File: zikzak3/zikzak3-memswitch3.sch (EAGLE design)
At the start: 45 parts, among them IC2 MEGA128-A, Q1 16MHz, Q2 20MHz

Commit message: updated schematic
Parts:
- added BUFFER3: 74LS245N, 74xx-us:74LS245N
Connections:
- new net N$105: BUFFER3A.A2, MUX10A.2Y
- new net N$106: BUFFER3A.A1, MUX10A.1Y
- new net N$109: BUFFER3A.A5, MUX9A.1Y
- new net N$11: BUFFER3A.A4, MUX10A.4Y
- new net N$110: BUFFER3A.A6, MUX9A.2Y
- new net N$111: BUFFER3A.A7, MUX9A.3Y
- new net N$112: BUFFER3A.A8, MUX9A.4Y
- new net N$12: MUX10A.3Y
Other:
- moved on the sheet: R10, R3, R4, R5, R6, R7, R8, R9
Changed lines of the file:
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@@
 <setting verticaltext="up"/>
 </settings>
-<grid distance="0.1" unitdist="inch" unit="inch" style="dots" multiple="1" display="yes" altdistance="0.01" altunitdist="inch" altunit="inch"/>
+<grid distance="0.1" unitdist="inch" unit="inch" style="lines" multiple="1" display="no" altdistance="0.01" altunitdist="inch" altunit="inch"/>
 <layers>
 <layer number="1" name="Top" color="4" fill="1" visible="no" active="no"/>
@@
 <part name="R10" library="rcl" deviceset="R-US_" device="0204/2V"/>
 <part name="INVERTOR" library="74xx-us" deviceset="74*04" device="N" technology="LS"/>
+<part name="BUFFER3" library="74xx-us" deviceset="74*245" device="N" technology="LS"/>
 </parts>
 <sheets>
@@
 <text x="243.84" y="63.5" size="6.4516" layer="91">GPU (Sync Gen)</text>
 <text x="302.26" y="-294.64" size="6.4516" layer="91">VGA</text>
-<text x="238.76" y="-294.64" size="6.4516" layer="91">DAC</text>
+<text x="266.7" y="-302.26" size="6.4516" layer="91">DAC</text>
 <text x="167.64" y="-299.72" size="6.4516" layer="91">VID SW</text>
 <text x="-170.18" y="-170.18" size="1.778" layer="91">INVERT</text>
@@
 <instance part="P+4" gate="1" x="30.48" y="-172.72"/>
 <instance part="GND14" gate="1" x="35.56" y="-154.94" rot="R180"/>
-<instance part="R3" gate="G$1" x="246.38" y="-228.6" rot="MR0"/>
-<instance part="R4" gate="G$1" x="246.38" y="-233.68" rot="MR0"/>
-<instance part="R5" gate="G$1" x="246.38" y="-243.84" rot="MR0"/>
-<instance part="R6" gate="G$1" x="246.38" y="-248.92" rot="MR0"/>
-<instance part="R7" gate="G$1" x="246.38" y="-261.62" rot="MR0"/>
-<instance part="R8" gate="G$1" x="246.38" y="-266.7" rot="MR0"/>
-<instance part="R9" gate="G$1" x="246.38" y="-276.86" rot="MR0"/>
-<instance part="R10" gate="G$1" x="246.38" y="-281.94" rot="MR0"/>
+<instance part="R3" gate="G$1" x="274.32" y="-236.22" rot="MR0"/>
+<instance part="R4" gate="G$1" x="274.32" y="-241.3" rot="MR0"/>
+<instance part="R5" gate="G$1" x="274.32" y="-251.46" rot="MR0"/>
+<instance part="R6" gate="G$1" x="274.32" y="-256.54" rot="MR0"/>
+<instance part="R7" gate="G$1" x="274.32" y="-269.24" rot="MR0"/>
+<instance part="R8" gate="G$1" x="274.32" y="-274.32" rot="MR0"/>
+<instance part="R9" gate="G$1" x="274.32" y="-284.48" rot="MR0"/>
+<instance part="R10" gate="G$1" x="274.32" y="-289.56" rot="MR0"/>
 <instance part="INVERTOR" gate="A" x="-167.64" y="-147.32" rot="R270"/>
+<instance part="BUFFER3" gate="A" x="233.68" y="-256.54"/>
 </instances>
 <busses>
@@
 </segment>
 </net>
-<net name="N$105" class="0">
-<segment>
-<wire x1="190.5" y1="-248.92" x2="236.22" y2="-248.92" width="0.1524" layer="91"/>
-</segment>
-</net>
-<net name="N$106" class="0">
-<segment>
-<wire x1="259.08" y1="-248.92" x2="299.72" y2="-248.92" width="0.1524" layer="91"/>
-</segment>
-</net>
 <net name="N$107" class="0">
 <segment>
@@
 </segment>
 </net>
+<net name="N$11" class="0">
+<segment>
+<pinref part="MUX10" gate="A" pin="4Y"/>
+<wire x1="187.96" y1="-238.76" x2="200.66" y2="-238.76" width="0.1524" layer="91"/>
+<wire x1="200.66" y1="-238.76" x2="200.66" y2="-251.46" width="0.1524" layer="91"/>
+<pinref part="BUFFER3" gate="A" pin="A4"/>
+<wire x1="200.66" y1="-251.46" x2="220.98" y2="-251.46" width="0.1524" layer="91"/>
+</segment>
+</net>
+<net name="N$12" class="0">
+<segment>
+<pinref part="MUX10" gate="A" pin="3Y"/>
+<wire x1="187.96" y1="-233.68" x2="203.2" y2="-233.68" width="0.1524" layer="91"/>
+<wire x1="203.2" y1="-233.68" x2="203.2" y2="-248.92" width="0.1524" layer="91"/>
+<wire x1="203.2" y1="-248.92" x2="223.52" y2="-248.92" width="0.1524" layer="91"/>
+</segment>
+</net>
+<net name="N$105" class="0">
+<segment>
+<pinref part="MUX10" gate="A" pin="2Y"/>
+<wire x1="187.96" y1="-228.6" x2="205.74" y2="-228.6" width="0.1524" layer="91"/>
+<wire x1="205.74" y1="-228.6" x2="205.74" y2="-246.38" width="0.1524" layer="91"/>
+<pinref part="BUFFER3" gate="A" pin="A2"/>
+<wire x1="205.74" y1="-246.38" x2="220.98" y2="-246.38" width="0.1524" layer="91"/>
+</segment>
+</net>
+<net name="N$106" class="0">
+<segment>
+<pinref part="MUX10" gate="A" pin="1Y"/>
+<wire x1="187.96" y1="-223.52" x2="208.28" y2="-223.52" width="0.1524" layer="91"/>
+<wire x1="208.28" y1="-223.52" x2="208.28" y2="-243.84" width="0.1524" layer="91"/>
+<pinref part="BUFFER3" gate="A" pin="A1"/>
+<wire x1="208.28" y1="-243.84" x2="220.98" y2="-243.84" width="0.1524" layer="91"/>
+</segment>
+</net>
+<net name="N$109" class="0">
+<segment>
+<pinref part="MUX9" gate="A" pin="1Y"/>
+<wire x1="200.66" y1="-259.08" x2="200.66" y2="-254" width="0.1524" layer="91"/>
+<pinref part="BUFFER3" gate="A" pin="A5"/>
+<wire x1="200.66" y1="-254" x2="220.98" y2="-254" width="0.1524" layer="91"/>
+</segment>
+</net>
+<net name="N$110" class="0">
+<segment>
+<pinref part="MUX9" gate="A" pin="2Y"/>
+<wire x1="200.66" y1="-264.16" x2="203.2" y2="-264.16" width="0.1524" layer="91"/>
+<wire x1="203.2" y1="-264.16" x2="203.2" y2="-256.54" width="0.1524" layer="91"/>
+<pinref part="BUFFER3" gate="A" pin="A6"/>
+<wire x1="203.2" y1="-256.54" x2="220.98" y2="-256.54" width="0.1524" layer="91"/>
+</segment>
+</net>
+<net name="N$111" class="0">
+<segment>
+<pinref part="MUX9" gate="A" pin="3Y"/>
+<wire x1="200.66" y1="-269.24" x2="205.74" y2="-269.24" width="0.1524" layer="91"/>
+<wire x1="205.74" y1="-269.24" x2="205.74" y2="-259.08" width="0.1524" layer="91"/>
+<pinref part="BUFFER3" gate="A" pin="A7"/>
+<wire x1="205.74" y1="-259.08" x2="220.98" y2="-259.08" width="0.1524" layer="91"/>
+</segment>
+</net>
+<net name="N$112" class="0">
+<segment>
+<pinref part="MUX9" gate="A" pin="4Y"/>
+<wire x1="200.66" y1="-274.32" x2="208.28" y2="-274.32" width="0.1524" layer="91"/>
+<wire x1="208.28" y1="-274.32" x2="208.28" y2="-261.62" width="0.1524" layer="91"/>
+<pinref part="BUFFER3" gate="A" pin="A8"/>
+<wire x1="208.28" y1="-261.62" x2="220.98" y2="-261.62" width="0.1524" layer="91"/>
+</segment>
+</net>

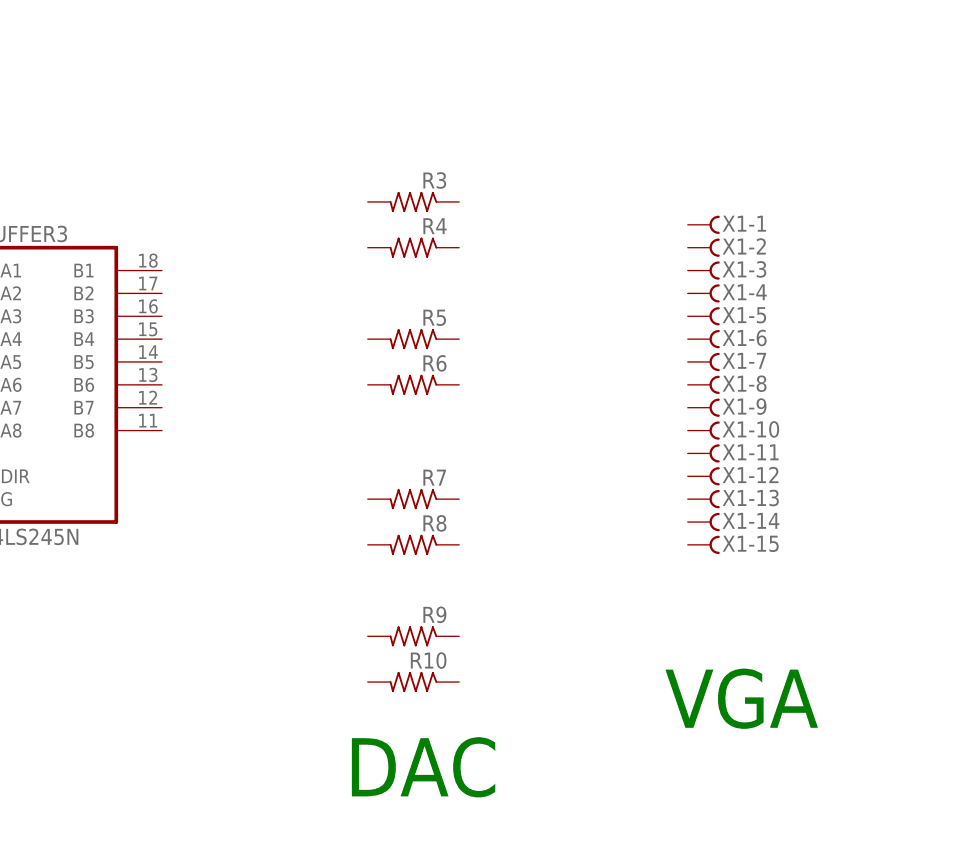
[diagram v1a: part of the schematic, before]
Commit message: schematic update; added DAC details
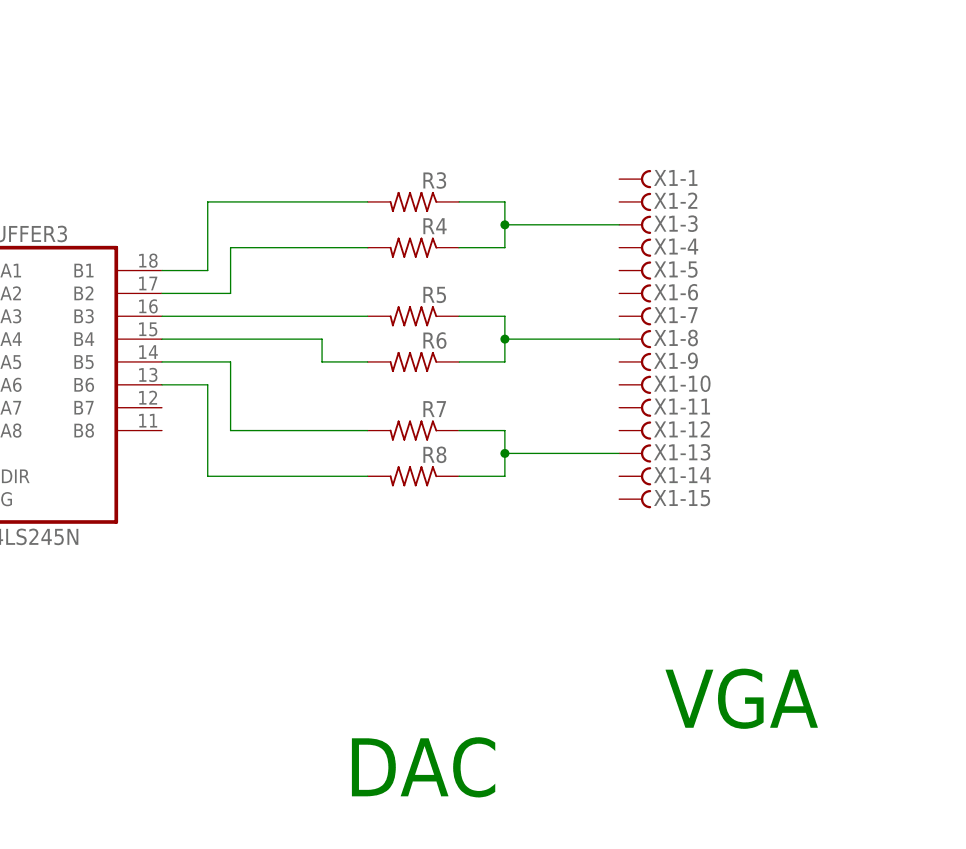
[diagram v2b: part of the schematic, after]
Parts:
- removed R10, R9: (no value), rcl:R-US_0204/2V
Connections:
- new net N$113: BUFFER3A.B1, R3.2
- new net N$114: BUFFER3A.B2, R4.2
- new net N$115: BUFFER3A.B3, R5.2
- new net N$116: BUFFER3A.B4, R6.2
- new net N$117: BUFFER3A.B5, R7.2
- new net N$118: BUFFER3A.B6, R8.2
- new net N$119: R3.1, R4.1, X1-3.F
- new net N$121: R5.1, R6.1, X1-8.F
- new net N$123: R7.1, R8.1, X1-13.F
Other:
- moved on the sheet: R5, R6, R7, R8, X1-1, X1-10, X1-11, X1-12, X1-13, X1-14, X1-15, X1-2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
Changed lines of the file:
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@@
 <part name="R7" library="rcl" deviceset="R-US_" device="0204/2V"/>
 <part name="R8" library="rcl" deviceset="R-US_" device="0204/2V"/>
-<part name="R9" library="rcl" deviceset="R-US_" device="0204/2V"/>
-<part name="R10" library="rcl" deviceset="R-US_" device="0204/2V"/>
 <part name="INVERTOR" library="74xx-us" deviceset="74*04" device="N" technology="LS"/>
 <part name="BUFFER3" library="74xx-us" deviceset="74*245" device="N" technology="LS"/>
@@
 <instance part="P+1" gate="1" x="-322.58" y="124.46" rot="MR0"/>
 <instance part="GND1" gate="1" x="-322.58" y="114.3" rot="MR0"/>
-<instance part="X1" gate="-1" x="307.34" y="-238.76"/>
-<instance part="X1" gate="-2" x="307.34" y="-241.3"/>
-<instance part="X1" gate="-3" x="307.34" y="-243.84"/>
-<instance part="X1" gate="-4" x="307.34" y="-246.38"/>
-<instance part="X1" gate="-5" x="307.34" y="-248.92"/>
-<instance part="X1" gate="-6" x="307.34" y="-251.46"/>
-<instance part="X1" gate="-7" x="307.34" y="-254"/>
-<instance part="X1" gate="-8" x="307.34" y="-256.54"/>
-<instance part="X1" gate="-9" x="307.34" y="-259.08"/>
-<instance part="X1" gate="-10" x="307.34" y="-261.62"/>
-<instance part="X1" gate="-11" x="307.34" y="-264.16"/>
-<instance part="X1" gate="-12" x="307.34" y="-266.7"/>
-<instance part="X1" gate="-13" x="307.34" y="-269.24"/>
-<instance part="X1" gate="-14" x="307.34" y="-271.78"/>
-<instance part="X1" gate="-15" x="307.34" y="-274.32"/>
+<instance part="X1" gate="-1" x="299.72" y="-233.68"/>
+<instance part="X1" gate="-2" x="299.72" y="-236.22"/>
+<instance part="X1" gate="-3" x="299.72" y="-238.76"/>
+<instance part="X1" gate="-4" x="299.72" y="-241.3"/>
+<instance part="X1" gate="-5" x="299.72" y="-243.84"/>
+<instance part="X1" gate="-6" x="299.72" y="-246.38"/>
+<instance part="X1" gate="-7" x="299.72" y="-248.92"/>
+<instance part="X1" gate="-8" x="299.72" y="-251.46"/>
+<instance part="X1" gate="-9" x="299.72" y="-254"/>
+<instance part="X1" gate="-10" x="299.72" y="-256.54"/>
+<instance part="X1" gate="-11" x="299.72" y="-259.08"/>
+<instance part="X1" gate="-12" x="299.72" y="-261.62"/>
+<instance part="X1" gate="-13" x="299.72" y="-264.16"/>
+<instance part="X1" gate="-14" x="299.72" y="-266.7"/>
+<instance part="X1" gate="-15" x="299.72" y="-269.24"/>
 <instance part="IC1" gate="A" x="-302.26" y="132.08" rot="MR0"/>
 <instance part="GND2" gate="1" x="-302.26" y="50.8" rot="R270"/>
@@
 <instance part="R3" gate="G$1" x="274.32" y="-236.22" rot="MR0"/>
 <instance part="R4" gate="G$1" x="274.32" y="-241.3" rot="MR0"/>
-<instance part="R5" gate="G$1" x="274.32" y="-251.46" rot="MR0"/>
-<instance part="R6" gate="G$1" x="274.32" y="-256.54" rot="MR0"/>
-<instance part="R7" gate="G$1" x="274.32" y="-269.24" rot="MR0"/>
-<instance part="R8" gate="G$1" x="274.32" y="-274.32" rot="MR0"/>
-<instance part="R9" gate="G$1" x="274.32" y="-284.48" rot="MR0"/>
-<instance part="R10" gate="G$1" x="274.32" y="-289.56" rot="MR0"/>
+<instance part="R5" gate="G$1" x="274.32" y="-248.92" rot="MR0"/>
+<instance part="R6" gate="G$1" x="274.32" y="-254" rot="MR0"/>
+<instance part="R7" gate="G$1" x="274.32" y="-261.62" rot="MR0"/>
+<instance part="R8" gate="G$1" x="274.32" y="-266.7" rot="MR0"/>
 <instance part="INVERTOR" gate="A" x="-167.64" y="-147.32" rot="R270"/>
 <instance part="BUFFER3" gate="A" x="233.68" y="-256.54"/>
@@
 </segment>
 </net>
+<net name="N$113" class="0">
+<segment>
+<pinref part="BUFFER3" gate="A" pin="B1"/>
+<wire x1="246.38" y1="-243.84" x2="251.46" y2="-243.84" width="0.1524" layer="91"/>
+<wire x1="251.46" y1="-243.84" x2="251.46" y2="-236.22" width="0.1524" layer="91"/>
+<pinref part="R3" gate="G$1" pin="2"/>
+<wire x1="251.46" y1="-236.22" x2="269.24" y2="-236.22" width="0.1524" layer="91"/>
+</segment>
+</net>
+<net name="N$114" class="0">
+<segment>
+<pinref part="BUFFER3" gate="A" pin="B2"/>
+<wire x1="246.38" y1="-246.38" x2="254" y2="-246.38" width="0.1524" layer="91"/>
+<wire x1="254" y1="-246.38" x2="254" y2="-241.3" width="0.1524" layer="91"/>
+<pinref part="R4" gate="G$1" pin="2"/>
+<wire x1="254" y1="-241.3" x2="269.24" y2="-241.3" width="0.1524" layer="91"/>
+</segment>
+</net>
+<net name="N$115" class="0">
+<segment>
+<pinref part="BUFFER3" gate="A" pin="B3"/>
+<wire x1="246.38" y1="-248.92" x2="269.24" y2="-248.92" width="0.1524" layer="91"/>
+<pinref part="R5" gate="G$1" pin="2"/>
+</segment>
+</net>
+<net name="N$116" class="0">
+<segment>
+<pinref part="BUFFER3" gate="A" pin="B4"/>
+<wire x1="246.38" y1="-251.46" x2="264.16" y2="-251.46" width="0.1524" layer="91"/>
+<wire x1="264.16" y1="-251.46" x2="264.16" y2="-254" width="0.1524" layer="91"/>
+<pinref part="R6" gate="G$1" pin="2"/>
+<wire x1="264.16" y1="-254" x2="269.24" y2="-254" width="0.1524" layer="91"/>
+</segment>
+</net>
+<net name="N$117" class="0">
+<segment>
+<pinref part="BUFFER3" gate="A" pin="B5"/>
+<wire x1="246.38" y1="-254" x2="254" y2="-254" width="0.1524" layer="91"/>
+<wire x1="254" y1="-254" x2="254" y2="-261.62" width="0.1524" layer="91"/>
+<pinref part="R7" gate="G$1" pin="2"/>
+<wire x1="254" y1="-261.62" x2="269.24" y2="-261.62" width="0.1524" layer="91"/>
+</segment>
+</net>
+<net name="N$118" class="0">
+<segment>
+<pinref part="BUFFER3" gate="A" pin="B6"/>
+<wire x1="246.38" y1="-256.54" x2="251.46" y2="-256.54" width="0.1524" layer="91"/>
+<wire x1="251.46" y1="-256.54" x2="251.46" y2="-266.7" width="0.1524" layer="91"/>
+<pinref part="R8" gate="G$1" pin="2"/>
+<wire x1="251.46" y1="-266.7" x2="269.24" y2="-266.7" width="0.1524" layer="91"/>
+</segment>
+</net>
+<net name="N$119" class="0">
+<segment>
+<pinref part="R3" gate="G$1" pin="1"/>
+<wire x1="279.4" y1="-236.22" x2="284.48" y2="-236.22" width="0.1524" layer="91"/>
+<wire x1="284.48" y1="-236.22" x2="284.48" y2="-238.76" width="0.1524" layer="91"/>
+<pinref part="X1" gate="-3" pin="F"/>
+<wire x1="284.48" y1="-238.76" x2="297.18" y2="-238.76" width="0.1524" layer="91"/>
+<pinref part="R4" gate="G$1" pin="1"/>
+<wire x1="279.4" y1="-241.3" x2="284.48" y2="-241.3" width="0.1524" layer="91"/>
+<wire x1="284.48" y1="-241.3" x2="284.48" y2="-238.76" width="0.1524" layer="91"/>
+<junction x="284.48" y="-238.76"/>
+</segment>
+</net>
+<net name="N$121" class="0">
+<segment>
+<pinref part="R5" gate="G$1" pin="1"/>
+<wire x1="279.4" y1="-248.92" x2="284.48" y2="-248.92" width="0.1524" layer="91"/>
+<wire x1="284.48" y1="-248.92" x2="284.48" y2="-251.46" width="0.1524" layer="91"/>
+<pinref part="X1" gate="-8" pin="F"/>
+<wire x1="284.48" y1="-251.46" x2="297.18" y2="-251.46" width="0.1524" layer="91"/>
+<pinref part="R6" gate="G$1" pin="1"/>
+<wire x1="279.4" y1="-254" x2="284.48" y2="-254" width="0.1524" layer="91"/>
+<wire x1="284.48" y1="-254" x2="284.48" y2="-251.46" width="0.1524" layer="91"/>
+<junction x="284.48" y="-251.46"/>
+</segment>
+</net>
+<net name="N$123" class="0">
+<segment>
+<pinref part="R7" gate="G$1" pin="1"/>
+<wire x1="279.4" y1="-261.62" x2="284.48" y2="-261.62" width="0.1524" layer="91"/>
+<wire x1="284.48" y1="-261.62" x2="284.48" y2="-264.16" width="0.1524" layer="91"/>
+<pinref part="X1" gate="-13" pin="F"/>
+<wire x1="284.48" y1="-264.16" x2="297.18" y2="-264.16" width="0.1524" layer="91"/>
+<pinref part="R8" gate="G$1" pin="1"/>
+<wire x1="279.4" y1="-266.7" x2="284.48" y2="-266.7" width="0.1524" layer="91"/>
+<wire x1="284.48" y1="-266.7" x2="284.48" y2="-264.16" width="0.1524" layer="91"/>
+<junction x="284.48" y="-264.16"/>
+</segment>
+</net>
